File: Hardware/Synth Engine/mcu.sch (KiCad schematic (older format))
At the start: 74 parts, among them J3 SWD_programming, J4 Capsense_0, J5 Capsense_1, J6 Capsense_2, J7 Capsense_3, SW10 SW_SPST, SW11 SW_SPST, SW12 SW_SPST, SW13 SW_SPST, SW2 SW_SPST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

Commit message: connect control board to main synth schem pages
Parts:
- removed R103, R104, R105, R106, R107, R108, R109, R110, R115, R116, R117, R118: R, digikey-footprints:0805, symbol R
- removed RV22, RV23, RV24, RV25, RV26, RV27, RV28, RV29: 20kA, Potentiometers:Potentiometer_Bourns_PTV09A-1_Horizontal, symbol POT
- removed RV30, RV31, RV32, RV33: 20kB, Potentiometers:Potentiometer_Bourns_PTV09A-1_Horizontal, symbol POT
- removed SW10, SW11, SW12, SW13, SW2, SW3, SW4, SW5, SW6, SW7, SW8, SW9: SW_SPST, SparkFun-Electromechanical:SWITCH-SPDT, symbol SW_SPST
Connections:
- net labels added: envelope_pwm_bypass_in_1, envelope_pwm_bypass_in_2, envelope_pwm_bypass_in_3, envelope_pwm_bypass_in_4, envelope_pwm_bypass_out_1, envelope_pwm_bypass_out_2, envelope_pwm_bypass_out_3, envelope_pwm_bypass_out_4
- wire segments 125 -> 113
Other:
- note removed: "Check tapers of speed control.\nI believe these should be linear."
- moved on the sheet: C90, C91, C92, C93, J3, R100, R101, R102, R111, R112, R113, R114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

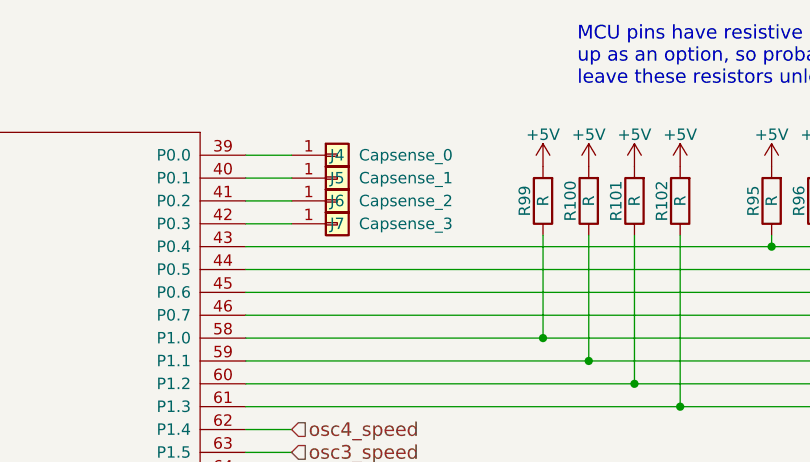
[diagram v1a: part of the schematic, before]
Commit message: add connectors for capsense buttons and LFO shape switch
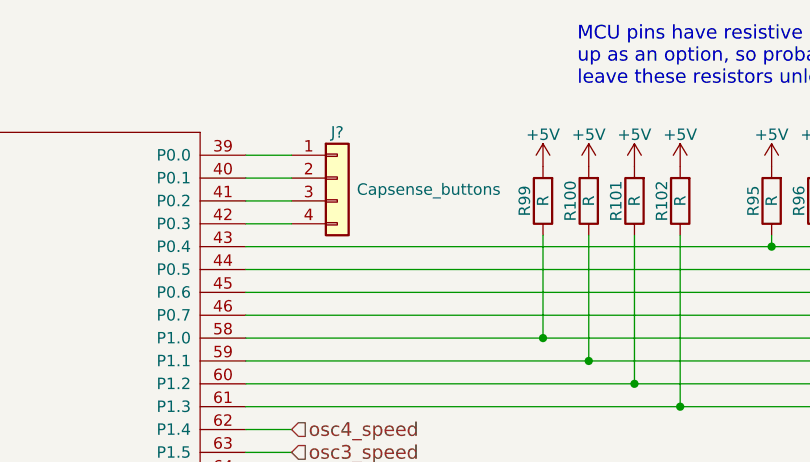
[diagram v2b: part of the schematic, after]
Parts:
- removed J4: Capsense_0, Cypress_capsense:Capsense_button, symbol Conn_01x01
- removed J5: Capsense_1, Cypress_capsense:Capsense_button, symbol Conn_01x01
- removed J6: Capsense_2, Cypress_capsense:Capsense_button, symbol Conn_01x01
- removed J7: Capsense_3, Cypress_capsense:Capsense_button, symbol Conn_01x01
- added J?: Capsense_buttons, symbol Conn_01x04
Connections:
- net at U6.39 (P0.0): now also J?.1 (Pin_1)
- net at U6.40 (P0.1): now also J?.2 (Pin_2)
- net at U6.41 (P0.2): now also J?.3 (Pin_3)
- net at U6.42 (P0.3): now also J?.4 (Pin_4)
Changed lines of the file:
@@
-$EndComp
-$Comp
-L Conn_01x01 J4
-U 1 1 5C3FE394
-P 5350 1200
-F 0 "J4" H 5350 1200 50  0000 C CNN
-F 1 "Capsense_0" H 5650 1200 50  0000 C CNN
-F 2 "Cypress_capsense:Capsense_button" H 5350 1200 50  0001 C CNN
-F 3 "" H 5350 1200 50  0001 C CNN
-	1    5350 1200
-	1    0    0    -1
-$EndComp
-$Comp
-L Conn_01x01 J5
-U 1 1 5C3FE689
-P 5350 1300
-F 0 "J5" H 5350 1300 50  0000 C CNN
-F 1 "Capsense_1" H 5650 1300 50  0000 C CNN
-F 2 "Cypress_capsense:Capsense_button" H 5350 1300 50  0001 C CNN
-F 3 "" H 5350 1300 50  0001 C CNN
-	1    5350 1300
-	1    0    0    -1
-$EndComp
-$Comp
-L Conn_01x01 J6
-U 1 1 5C3FE726
-P 5350 1400
-F 0 "J6" H 5350 1400 50  0000 C CNN
-F 1 "Capsense_2" H 5650 1400 50  0000 C CNN
-F 2 "Cypress_capsense:Capsense_button" H 5350 1400 50  0001 C CNN
-F 3 "" H 5350 1400 50  0001 C CNN
-	1    5350 1400
-	1    0    0    -1
-$EndComp
-$Comp
-L Conn_01x01 J7
-U 1 1 5C3FE7BA
-P 5350 1500
-F 0 "J7" H 5350 1500 50  0000 C CNN
-F 1 "Capsense_3" H 5650 1500 50  0000 C CNN
-F 2 "Cypress_capsense:Capsense_button" H 5350 1500 50  0001 C CNN
-F 3 "" H 5350 1500 50  0001 C CNN
-	1    5350 1500
-	1    0    0    -1
 $EndComp
 $Comp
@@
 	9050 4450 9050 5200
 Connection ~ 9050 5200
+$Comp
+L Conn_01x04 J?
+U 1 1 5C5E2C0E
+P 5350 1300
+F 0 "J?" H 5350 1500 50  0000 C CNN
+F 1 "Capsense_buttons" H 5750 1250 50  0000 C CNN
+F 2 "" H 5350 1300 50  0001 C CNN
+F 3 "" H 5350 1300 50  0001 C CNN
+	1    5350 1300
+	1    0    0    -1
+$EndComp
 $EndSCHEMATC

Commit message: remove extraneous net labels
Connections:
- net envelope_pwm_1: no longer R111.2, U6.51 (P5.0)
- net envelope_pwm_2: no longer R112.2, U6.52 (P5.1)
- net envelope_pwm_3: no longer R113.2, U6.53 (P5.2)
- net envelope_pwm_4: no longer R114.2, U6.54 (P5.3)
- new net envelope_pwm_bypass_in_1: R111.2, U6.51 (P5.0)
- new net envelope_pwm_bypass_in_2: R112.2, U6.52 (P5.1)
- new net envelope_pwm_bypass_in_3: R113.2, U6.53 (P5.2)
- new net envelope_pwm_bypass_in_4: R114.2, U6.54 (P5.3)
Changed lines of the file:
@@
 Text HLabel 9450 5200 2    60   Output ~ 0
-envelope_pwm_4
-Text Label 5150 4900 0    60   ~ 0
-envelope_pwm_1
-Text Label 5150 5000 0    60   ~ 0
-envelope_pwm_2
-Text Label 5150 5100 0    60   ~ 0
-envelope_pwm_3
-Text Label 5150 5200 0    60   ~ 0
-envelope_pwm_4
-Text Label 7400 4900 2    60   ~ 0
-envelope_pwm_1
-Text Label 7400 5000 2    60   ~ 0
-envelope_pwm_2
-Text Label 7400 5100 2    60   ~ 0
-envelope_pwm_3
-Text Label 7400 5200 2    60   ~ 0
 envelope_pwm_4
 $Comp
@@
 	4950 5700 5150 5700
 Wire Wire Line
-	5150 4900 4950 4900
-Wire Wire Line
-	5150 5000 4950 5000
-Wire Wire Line
-	4950 5100 5150 5100
-Wire Wire Line
-	4950 5200 5150 5200
+	4950 4900 8000 4900
+Wire Wire Line
+	4950 5000 8000 5000
+Wire Wire Line
+	4950 5100 8000 5100
+Wire Wire Line
+	4950 5200 8000 5200
 Wire Wire Line
 	750  6150 750  6300
@@
 Connection ~ 8950 5200
 Wire Wire Line
-	7400 4900 8000 4900
-Wire Wire Line
-	7400 5000 8000 5000
-Wire Wire Line
-	7400 5100 8000 5100
-Wire Wire Line
-	7400 5200 8000 5200
-Wire Wire Line
 	4950 1600 7950 1600

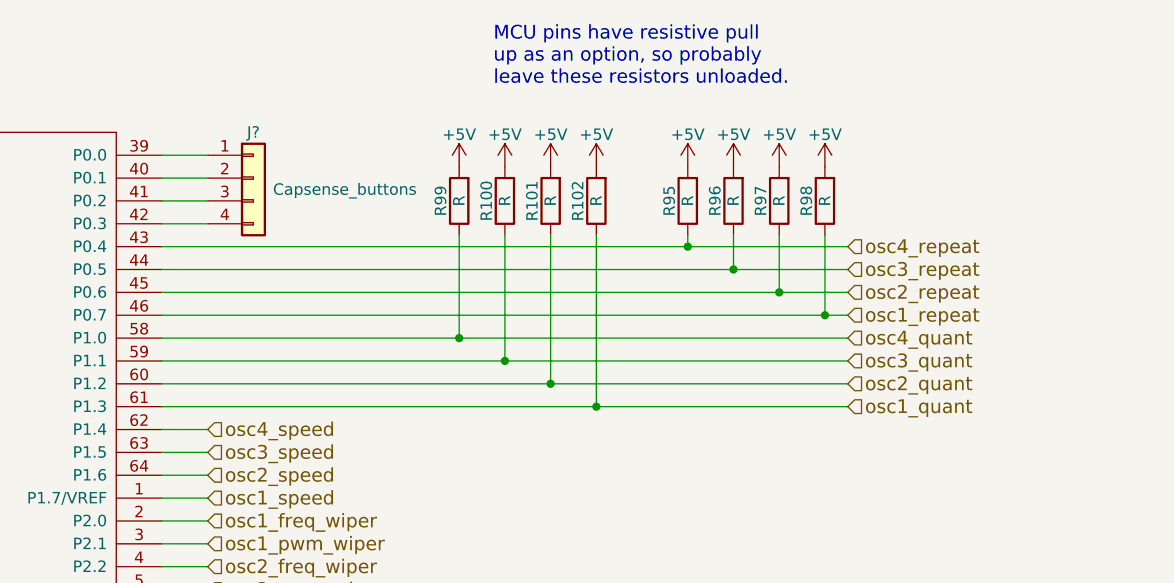
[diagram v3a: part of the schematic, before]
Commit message: remove external pull-up resistors on digital input pins. These are unecessary due to internal pull-up resistors.
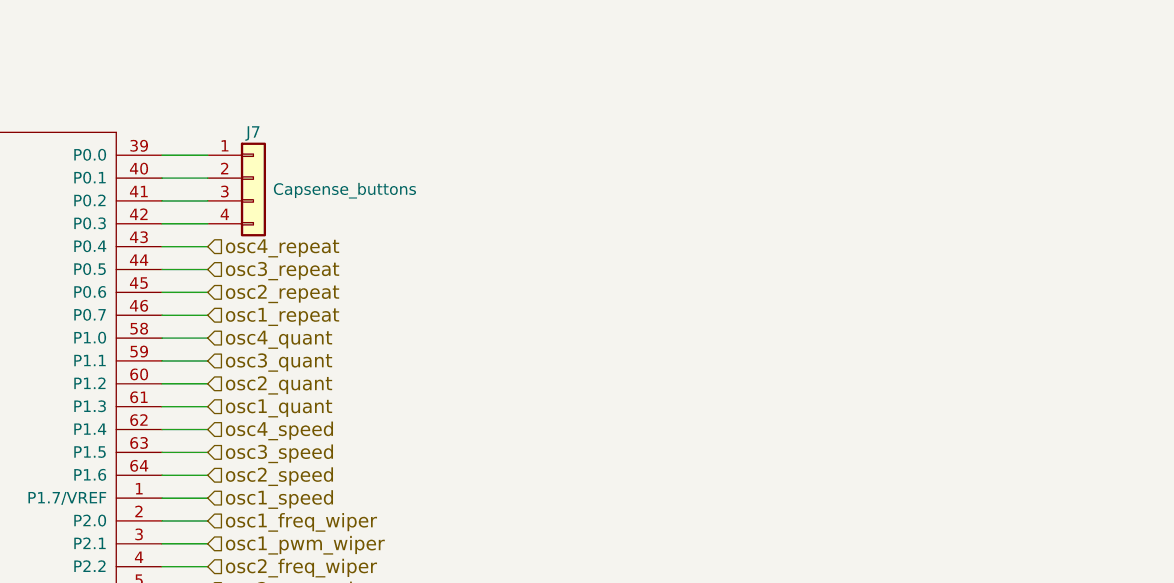
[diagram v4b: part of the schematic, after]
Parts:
- removed R100, R101, R102, R95, R96, R97, R98, R99: R, digikey-footprints:0805, symbol R
- C78, C79, C83, C86, C88: footprint Capacitors_SMD:CP_Elec_4x4.5 -> digikey-footprints:0805
- J7: renamed from J?; footprint (none) -> Pin_Headers:Pin_Header_Straight_1x04_Pitch2.54mm
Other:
- note removed: "MCU pins have resistive pull \nup as an option, so probably \nleave these resistors unloaded."

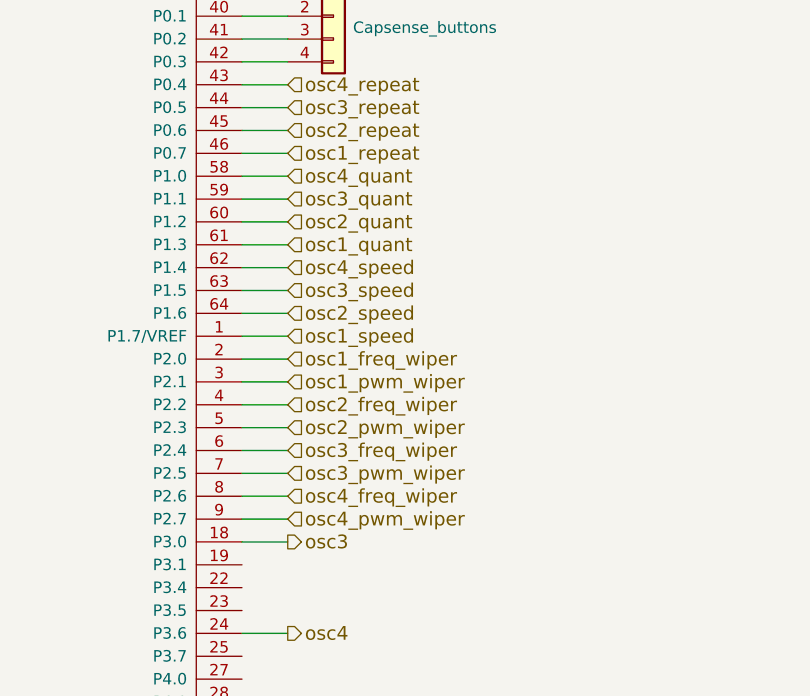
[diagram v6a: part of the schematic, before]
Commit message: correct placement of filter connectors, and they are placed relative to the ADC connectors. This should result in mating connection between both boards.
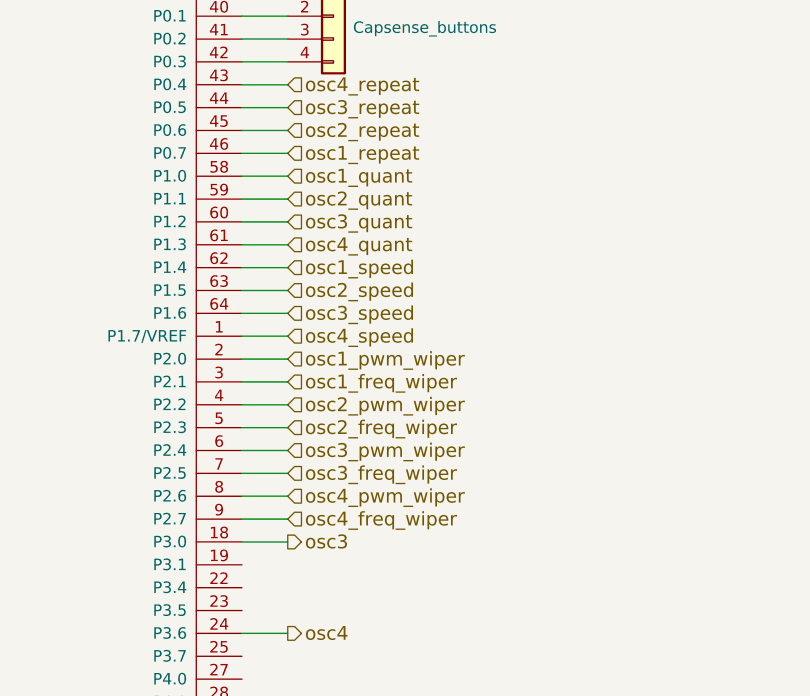
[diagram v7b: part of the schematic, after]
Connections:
- net osc1_freq_wiper: now also U6.3 (P2.1); no longer U6.2 (P2.0)
- net osc1_pwm_wiper: now also U6.2 (P2.0); no longer U6.3 (P2.1)
- net osc1_quant: now also U6.58 (P1.0); no longer U6.61 (P1.3)
- net osc1_speed: now also U6.62 (P1.4); no longer U6.1 (P1.7/VREF)
- net osc2_freq_wiper: now also U6.5 (P2.3); no longer U6.4 (P2.2)
- net osc2_pwm_wiper: now also U6.4 (P2.2); no longer U6.5 (P2.3)
- net osc2_quant: now also U6.59 (P1.1); no longer U6.60 (P1.2)
- net osc2_speed: now also U6.63 (P1.5); no longer U6.64 (P1.6)
- net osc3_freq_wiper: now also U6.7 (P2.5); no longer U6.6 (P2.4)
- net osc3_pwm_wiper: now also U6.6 (P2.4); no longer U6.7 (P2.5)
- net osc3_quant: now also U6.60 (P1.2); no longer U6.59 (P1.1)
- net osc3_speed: now also U6.64 (P1.6); no longer U6.63 (P1.5)
- net osc4_freq_wiper: now also U6.9 (P2.7); no longer U6.8 (P2.6)
- net osc4_pwm_wiper: now also U6.8 (P2.6); no longer U6.9 (P2.7)
- net osc4_quant: now also U6.61 (P1.3); no longer U6.58 (P1.0)
- net osc4_speed: now also U6.1 (P1.7/VREF); no longer U6.62 (P1.4)
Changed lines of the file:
@@
 	1    0    0    -1
 $EndComp
+Text HLabel 5150 2900 2    60   Input ~ 0
+osc1_freq_wiper
 Text HLabel 5150 2800 2    60   Input ~ 0
-osc1_freq_wiper
-Text HLabel 5150 2900 2    60   Input ~ 0
 osc1_pwm_wiper
+Text HLabel 5150 3100 2    60   Input ~ 0
+osc2_freq_wiper
 Text HLabel 5150 3000 2    60   Input ~ 0
-osc2_freq_wiper
-Text HLabel 5150 3100 2    60   Input ~ 0
 osc2_pwm_wiper
+Text HLabel 5150 3300 2    60   Input ~ 0
+osc3_freq_wiper
 Text HLabel 5150 3200 2    60   Input ~ 0
-osc3_freq_wiper
-Text HLabel 5150 3300 2    60   Input ~ 0
 osc3_pwm_wiper
+Text HLabel 5150 3500 2    60   Input ~ 0
+osc4_freq_wiper
 Text HLabel 5150 3400 2    60   Input ~ 0
-osc4_freq_wiper
-Text HLabel 5150 3500 2    60   Input ~ 0
 osc4_pwm_wiper
+Text HLabel 5150 2400 2    60   Input ~ 0
+osc1_speed
+Text HLabel 5150 2500 2    60   Input ~ 0
+osc2_speed
+Text HLabel 5150 2600 2    60   Input ~ 0
+osc3_speed
 Text HLabel 5150 2700 2    60   Input ~ 0
-osc1_speed
-Text HLabel 5150 2600 2    60   Input ~ 0
-osc2_speed
-Text HLabel 5150 2500 2    60   Input ~ 0
-osc3_speed
-Text HLabel 5150 2400 2    60   Input ~ 0
 osc4_speed
+Text HLabel 5150 2000 2    60   Input ~ 0
+osc1_quant
+Text HLabel 5150 2100 2    60   Input ~ 0
+osc2_quant
+Text HLabel 5150 2200 2    60   Input ~ 0
+osc3_quant
 Text HLabel 5150 2300 2    60   Input ~ 0
-osc1_quant
-Text HLabel 5150 2200 2    60   Input ~ 0
-osc2_quant
-Text HLabel 5150 2100 2    60   Input ~ 0
-osc3_quant
-Text HLabel 5150 2000 2    60   Input ~ 0
 osc4_quant
 Text HLabel 5150 1900 2    60   Input ~ 0
